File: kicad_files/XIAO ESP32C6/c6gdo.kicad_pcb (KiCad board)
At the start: 2 copper layers, 28.4 x 21 mm, 11 parts, among them J1 250-1402, Q1 2N7002, Q2 AO3400A, U1 XIAO-ESP32-C6-SMD

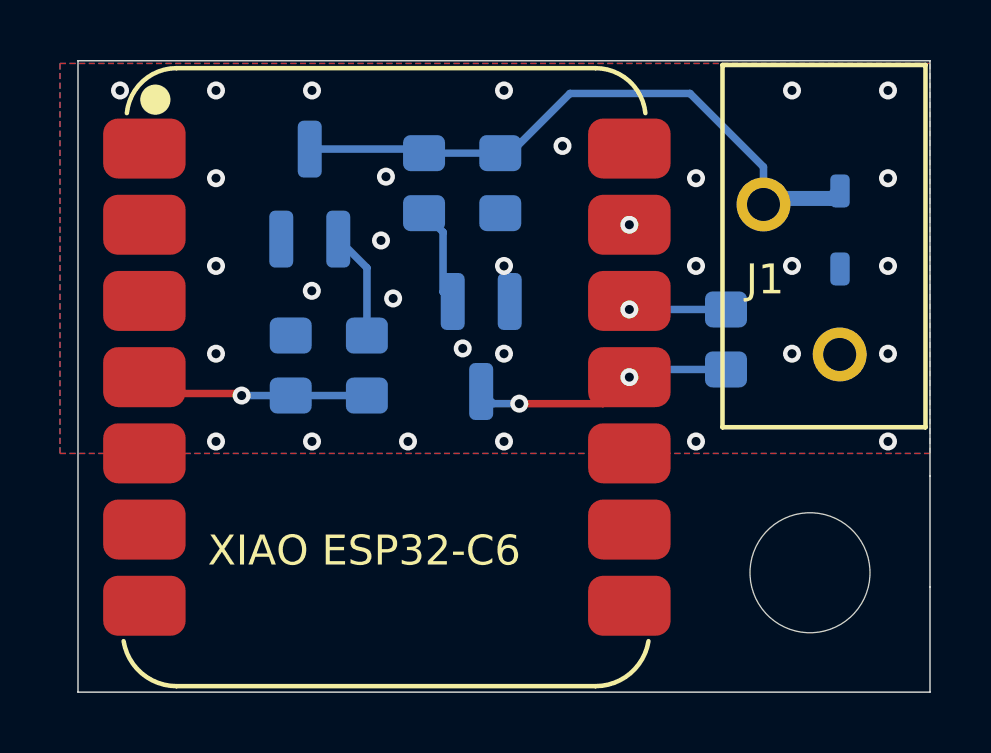
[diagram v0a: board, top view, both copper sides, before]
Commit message: Add C5 support
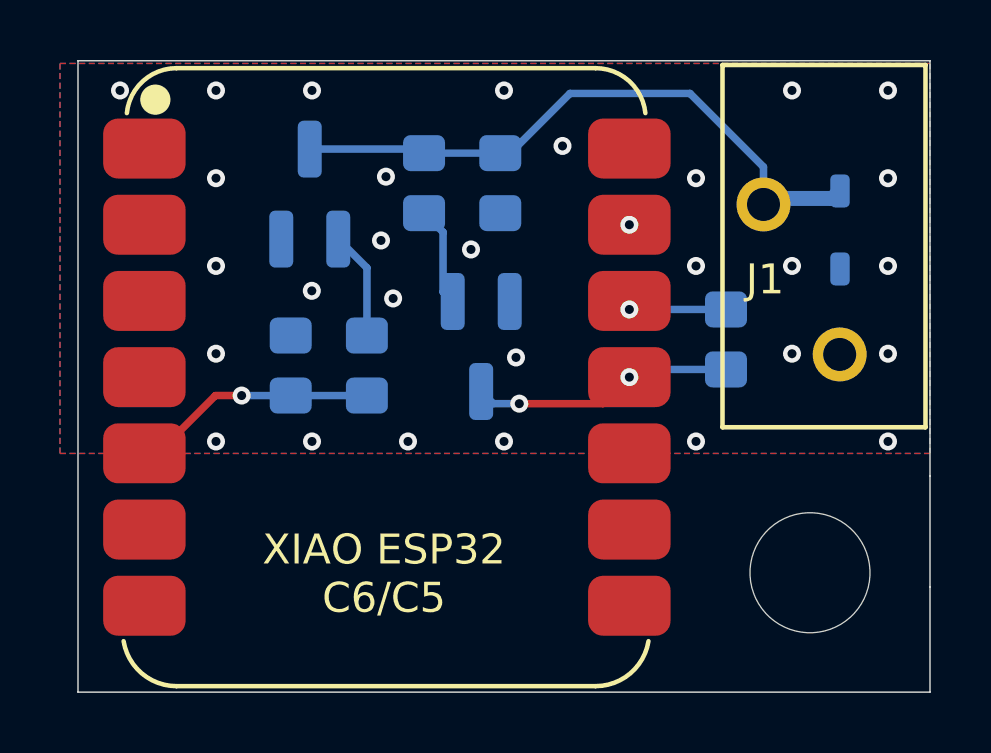
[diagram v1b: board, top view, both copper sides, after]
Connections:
- U1 pad 4: /ESP_TX -> unconnected-(U1-GPIO21_D3-Pad4)
- U1 pad 5: unconnected-(U1-GPIO22_D4_SDA-Pad5) -> /ESP_TX
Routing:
- net /ESP_TX: track 7.67 -> 8.21 mm
- net GND: vias 31 -> 30
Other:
- board text added: "XIAO ESP32 C6/C5"
- board text removed: "XIAO ESP32-C6"
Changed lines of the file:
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@@
 		)
 		(fp_circle
-			(center 10.064 -11.5783)
-			(end 10.914 -11.5783)
+			(center 10.151 -11.4937)
+			(end 11.001 -11.4937)
 			(stroke
 				(width 0.1)
@@
 			(layers "F.Cu" "F.Mask" "F.Paste")
 			(roundrect_rratio 0.25)
-			(net "/ESP_TX")
+			(net "unconnected-(U1-GPIO21_D3-Pad4)")
 			(pinfunction "GPIO21_D3_4")
 			(pintype "passive")
@@
 			(layers "F.Cu" "F.Mask" "F.Paste")
 			(roundrect_rratio 0.25)
-			(net "unconnected-(U1-GPIO22_D4_SDA-Pad5)")
+			(net "/ESP_TX")
 			(pinfunction "GPIO22_D4_SDA_5")
 			(pintype "passive")
@@
 			(polygon
 				(pts
-					(xy 65.1424 51.3782) (xy 65.0587 51.7992) (xy 64.8202 52.156) (xy 64.4634 52.3945) (xy 64.0424 52.4782)
-					(xy 63.6214 52.3945) (xy 63.2646 52.156) (xy 63.0261 51.7992) (xy 62.9424 51.3782) (xy 63.0261 50.9572)
-					(xy 63.2646 50.6004) (xy 63.6214 50.3619) (xy 64.0424 50.2782) (xy 64.4634 50.3619) (xy 64.8202 50.6004)
-					(xy 65.0587 50.9572)
+					(xy 65.2294 51.4628) (xy 65.1457 51.8838) (xy 64.9072 52.2406) (xy 64.5504 52.4791) (xy 64.1294 52.5628)
+					(xy 63.7084 52.4791) (xy 63.3516 52.2406) (xy 63.1131 51.8838) (xy 63.0294 51.4628) (xy 63.1131 51.0418)
+					(xy 63.3516 50.685) (xy 63.7084 50.4465) (xy 64.1294 50.3628) (xy 64.5504 50.4465) (xy 64.9072 50.685)
+					(xy 65.1457 51.0418)
 				)
 			)
@@
 		(layer "Edge.Cuts")
 	)
-	(gr_text "XIAO ESP32-C6"
-		(at 56.925 58.825 0)
+	(gr_text "XIAO ESP32\nC6/C5"
+		(at 62.8 60.4 0)
 		(layer "F.SilkS")
 		(effects
@@
 				(thickness 0.15)
 			)
-			(justify left bottom)
+			(justify bottom)
 		)
 	)
@@
 	)
 	(via
-		(at 66.8 48.75)
+		(at 65.7 48.2)
 		(size 0.6)
 		(drill 0.3)
@@
 	)
 	(via
-		(at 65.424218 51.49919)
-		(size 0.6)
-		(drill 0.3)
-		(layers "F.Cu" "B.Cu")
-		(free yes)
-		(net "GND")
-	)
-	(via
 		(at 73.2 54.6)
 		(size 0.6)
@@
 	)
 	(via
-		(at 66.8 51.675)
+		(at 67.2 51.8)
 		(size 0.6)
 		(drill 0.3)
@@
 	)
 	(segment
-		(start 57.985 53)
-		(end 55.3569 53)
+		(start 55.2535 54.9965)
+		(end 54.8134 54.9965)
 		(width 0.25)
 		(layer "F.Cu")
@@
 	)
 	(segment
-		(start 55.3569 53)
-		(end 54.8134 52.4565)
+		(start 57.18 53.07)
+		(end 55.2535 54.9965)
 		(width 0.25)
 		(layer "F.Cu")
@@
 	(segment
 		(start 58.055 53.07)
-		(end 57.985 53)
+		(end 57.18 53.07)
 		(width 0.25)
 		(layer "F.Cu")

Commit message: D1 with better clamping voltage
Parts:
- D1: value CDSOD323-T15S -> PTVS15VS1UR; footprint c6gdo:D_SOD-323 -> c6gdo:Nexperia_CFP3_SOD-123W
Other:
- board text added: "MFLAGG 2026 V1.1"
- board text removed: "MFLAGG 2026 V1.0"
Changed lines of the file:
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@@
 	(title_block
 		(title "XIAO ESP32-C6 Security+ 2.0 Garage Door Interface")
-		(date "2026-09-16")
-		(rev "1.0")
+		(date "2026-09-17")
+		(rev "1.1")
 		(company "MFLAGG")
 	)
@@
 			)
 		)
-		(property "Digi-Key PN" "2946-250-1402-ND"
+		(property "DigiKey PN" "2946-250-1402-ND"
 			(at 0 0 0)
 			(unlocked yes)
@@
 			)
 		)
-		(property "Digi-Key PN" "1597-113991254-ND"
+		(property "DigiKey PN" "1597-113991254-ND"
 			(at 0 0 0)
 			(unlocked yes)
@@
 			)
 		)
-		(property "Digi-Key PN" "RPC7858-ND"
+		(property "DigiKey PN" "RPC7858-ND"
 			(at 0 0 0)
 			(unlocked yes)
@@
 			)
 		)
-		(property "Digi-Key PN" "P123794CT-ND"
+		(property "DigiKey PN" "P123794CT-ND"
 			(at 0 0 0)
 			(unlocked yes)
@@
 			)
 		)
-		(property "Digi-Key PN" "785-1000-1-ND"
+		(property "DigiKey PN" "785-1000-1-ND"
 			(at 0 0 0)
 			(unlocked yes)
@@
 		)
 	)
-	(footprint "c6gdo:D_SOD-323"
+	(footprint "c6gdo:Nexperia_CFP3_SOD-123W"
 		(layer "B.Cu")
 		(at 78 47.55 -90)
-		(descr "SOD-323, enlarged pads for hand soldering")
-		(tags "SOD-323 handsolder")
+		(descr "Nexperia CFP3 (SOD-123W), https://assets.nexperia.com/documents/outline-drawing/SOD123W.pdf")
+		(tags "CFP3 SOD-123W")
 		(property "Reference" "D1"
 			(at 0 -1.75 90)
@@
 			)
 		)
-		(property "Value" "CDSOD323-T15S"
+		(property "Value" "PTVS15VS1UR"
 			(at 0.1 -1.9 90)
 			(layer "B.Fab")
@@
 			)
 		)
-		(property "Datasheet" "https://www.bourns.com/docs/product-datasheets/cdsod323-txxsc.pdf"
+		(property "Datasheet" "https://assets.nexperia.com/documents/data-sheet/PTVSXS1UR_SER.pdf"
 			(at 0 0 90)
 			(unlocked yes)
@@
 			)
 		)
-		(property "Description" "15V unidirectional TVS, SOD-323"
+		(property "Description" "15V 400W unidirectional TVS, SOD-123W"
 			(at 0 0 90)
 			(unlocked yes)
@@
 			)
 		)
-		(property "Manufacturer" "Bourns Inc."
+		(property "Manufacturer" "Nexperia"
 			(at 0 0 0)
 			(unlocked yes)
@@
 			)
 		)
-		(property "MPN" "CDSOD323-T15S"
+		(property "MPN" "PTVS15VS1UR,115"
 			(at 0 0 0)
 			(unlocked yes)
@@
 			)
 		)
-		(property "Digi-Key PN" "CDSOD323-T15SCT-ND"
+		(property "DigiKey PN" "1727-5315-1-ND"
 			(at 0 0 0)
 			(unlocked yes)
@@
 			)
 		)
-		(property ki_fp_filters "D*SOD?323*")
+		(property ki_fp_filters "*SOD?123W*")
 		(sheetname "/")
 		(sheetfile "c6gdo.kicad_sch")
@@
 		(duplicate_pad_numbers_are_jumpers no)
 		(fp_line
-			(start -2.01 0.85)
-			(end 1.05 0.85)
+			(start -2.26 0.95)
+			(end 1.4 0.95)
 			(stroke
 				(width 0.12)
@@
 		)
 		(fp_line
-			(start -2.01 0.85)
-			(end -2.01 -0.85)
+			(start -2.26 0.95)
+			(end -2.26 -0.95)
 			(stroke
 				(width 0.12)
@@
 		)
 		(fp_line
-			(start -2.01 -0.85)
-			(end 1.05 -0.85)
+			(start -2.26 -0.95)
+			(end 1.4 -0.95)
 			(stroke
 				(width 0.12)
@@
 		)
 		(fp_line
-			(start -2.1 0.95)
-			(end 2.1 0.95)
+			(start -2.25 1.1)
+			(end 2.25 1.1)
 			(stroke
 				(width 0.05)
@@
 		)
 		(fp_line
-			(start -2.1 0.95)
-			(end -2.1 -0.95)
+			(start -2.25 1.1)
+			(end -2.25 -1.1)
 			(stroke
 				(width 0.05)
@@
 		)
 		(fp_line
-			(start 2.1 0.95)
-			(end 2.1 -0.95)
+			(start 2.25 1.1)
+			(end 2.25 -1.1)
 			(stroke
 				(width 0.05)
@@
 		)
 		(fp_line
-			(start -2.1 -0.95)
-			(end 2.1 -0.95)
+			(start 2.25 -1.1)
+			(end -2.25 -1.1)
 			(stroke
 				(width 0.05)
@@
 		)
 		(fp_line
-			(start -0.9 0.7)
-			(end 0.9 0.7)
+			(start -1.3 0.85)
+			(end 1.3 0.85)
 			(stroke
 				(width 0.1)
@@
 		)
 		(fp_line
-			(start 0.9 0.7)
-			(end 0.9 -0.7)
+			(start 1.3 0.85)
+			(end 1.3 -0.85)
 			(stroke
 				(width 0.1)
@@
 		)
 		(fp_line
-			(start -0.3 0.35)
-			(end -0.3 -0.35)
+			(start -0.35 0.55)
+			(end -0.35 -0.55)
 			(stroke
 				(width 0.1)
@@
 		)
 		(fp_line
-			(start 0.2 0.35)
-			(end 0.2 -0.35)
+			(start 0.25 0.4)
+			(end 0.25 -0.4)
 			(stroke
 				(width 0.1)
@@
 		)
 		(fp_line
-			(start -0.3 0)
-			(end 0.2 0.35)
+			(start -0.75 0)
+			(end -0.35 0)
 			(stroke
 				(width 0.1)
@@
 		)
 		(fp_line
-			(start -0.3 0)
-			(end -0.5 0)
+			(start -0.35 0)
+			(end 0.25 0.4)
 			(stroke
 				(width 0.1)
@@
 		)
 		(fp_line
-			(start 0.2 0)
-			(end 0.45 0)
+			(start -0.35 0)
+			(end 0.25 -0.4)
 			(stroke
 				(width 0.1)
@@
 		)
 		(fp_line
-			(start 0.2 -0.35)
-			(end -0.3 0)
+			(start 0.75 0)
+			(end 0.25 0)
 			(stroke
 				(width 0.1)
@@
 		)
 		(fp_line
-			(start -0.9 -0.7)
-			(end -0.9 0.7)
+			(start -1.3 -0.85)
+			(end -1.3 0.85)
 			(stroke
 				(width 0.1)
@@
 		)
 		(fp_line
-			(start 0.9 -0.7)
-			(end -0.9 -0.7)
+			(start 1.3 -0.85)
+			(end -1.3 -0.85)
 			(stroke
 				(width 0.1)
@@
 			)
 		)
-		(pad "1" smd roundrect
-			(at -1.3 0 270)
-			(size 1.1 0.65)
+		(pad "1" smd rect
+			(at -1.4 0 270)
+			(size 1.2 1.2)
 			(layers "B.Cu" "B.Mask" "B.Paste")
-			(roundrect_rratio 0.25)
 			(net "RED{slash}CTRL")
 			(pinfunction "K_1")
 			(pintype "passive")
 		)
-		(pad "2" smd roundrect
-			(at 1.3 0 270)
-			(size 1.1 0.65)
+		(pad "2" smd rect
+			(at 1.4 0 270)
+			(size 1.2 1.2)
 			(layers "B.Cu" "B.Mask" "B.Paste")
-			(roundrect_rratio 0.25)
 			(net "GND")
 			(pinfunction "A_2")
@@
 		)
 		(embedded_fonts no)
-		(model "${KIPRJMOD}/lib/c6gdo.3dshapes/D_SOD-323.step"
+		(model "${KIPRJMOD}/lib/c6gdo.3dshapes/Nexperia_CFP3_SOD-123W.step"
 			(offset
 				(xyz 0 0 0)
@@
 			)
 		)
-		(property "Digi-Key PN" "P1.0KDACT-ND"
+		(property "DigiKey PN" "P1.0KDACT-ND"
 			(at 0 0 0)
 			(unlocked yes)
@@
 			)
 		)
-		(property "Digi-Key PN" "P123794CT-ND"
+		(property "DigiKey PN" "P123794CT-ND"
 			(at 0 0 0)
 			(unlocked yes)
@@
 			)
 		)
-		(property "Digi-Key PN" "P4.7KDACT-ND"
+		(property "DigiKey PN" "P4.7KDACT-ND"
 			(at 0 0 0)
 			(unlocked yes)
@@
 			)
 		)
-		(property "Digi-Key PN" "2N7002NCT-ND"
+		(property "DigiKey PN" "2N7002NCT-ND"
 			(at 0 0 0)
 			(unlocked yes)
@@
 			)
 		)
-		(property "Digi-Key PN" "P100KDACT-ND"
+		(property "DigiKey PN" "P100KDACT-ND"
 			(at 0 0 0)
 			(unlocked yes)
@@
 		)
 	)
-	(gr_text "MFLAGG 2026\nV1.0"
+	(gr_text "MFLAGG 2026\nV1.1"
 		(at 63 60.425 0)
 		(layer "B.SilkS")
